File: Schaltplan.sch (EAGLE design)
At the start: 58 parts, among them Q1 TN0602N3, Q10 TN0602N3, Q11 TN0602N3, Q12 TN0602N3, Q13 TN0602N3, Q14 TN0602N3, Q15 TN0602N3, Q16 TN0602N3, Q17 TN0602N3, Q18 TN0602N3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

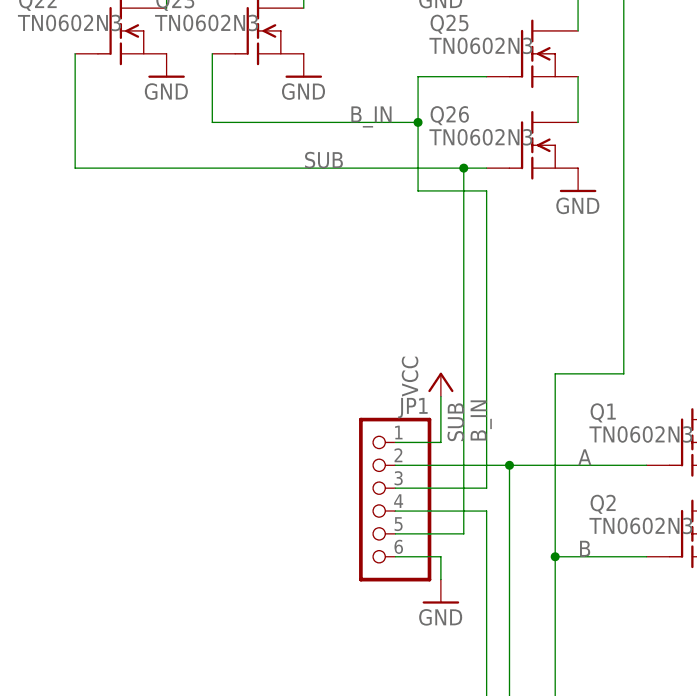
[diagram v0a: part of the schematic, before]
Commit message: Added Pull-Up Resistors
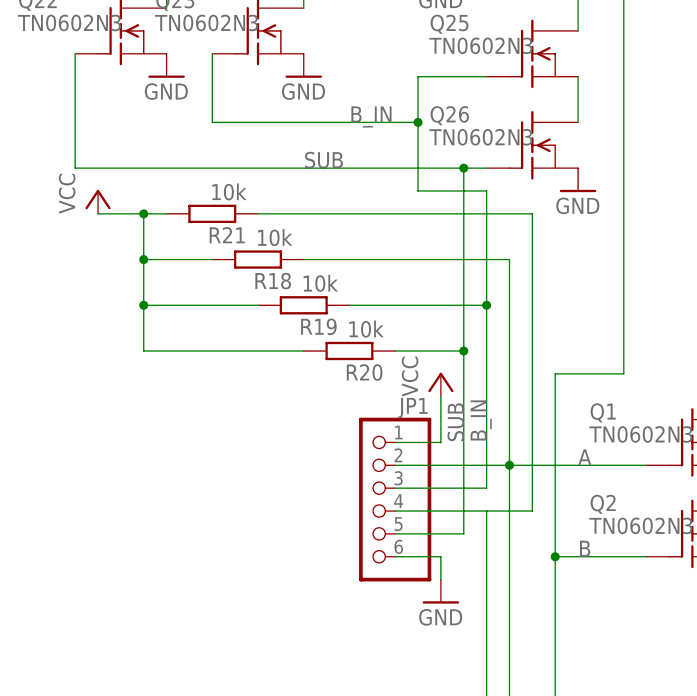
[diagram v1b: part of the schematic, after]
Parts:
- removed U$1, U$2: LOGO, logo:LOGO
- added R18, R19, R20, R21: 10k, resistor:R-EU_M0805
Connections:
- net A: now also R18.1
- net B_IN: now also R19.1
- net C_IN: now also R21.1
- net SUB: now also R20.1
- net VCC: now also R18.2, R19.2, R20.2, R21.2
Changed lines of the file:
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@@
 <part name="GND27" library="supply1" deviceset="GND" device=""/>
 <part name="GND28" library="supply1" deviceset="GND" device=""/>
-<part name="U$1" library="logo" deviceset="LOGO" device=""/>
-<part name="U$2" library="logo" deviceset="LOGO" device=""/>
 <part name="U$3" library="logo" deviceset="LOGO" device=""/>
+<part name="R18" library="resistor" deviceset="R-EU_" device="M0805" value="10k"/>
+<part name="R19" library="resistor" deviceset="R-EU_" device="M0805" value="10k"/>
+<part name="R20" library="resistor" deviceset="R-EU_" device="M0805" value="10k"/>
+<part name="R21" library="resistor" deviceset="R-EU_" device="M0805" value="10k"/>
+<part name="P+23" library="supply1" deviceset="VCC" device=""/>
 </parts>
 <sheets>
@@
 <instance part="GND28" gate="1" x="139.7" y="144.78"/>
 <instance part="U$3" gate="G$1" x="2.54" y="45.72"/>
+<instance part="R18" gate="G$1" x="7.62" y="114.3" rot="R180"/>
+<instance part="R19" gate="G$1" x="12.7" y="109.22" rot="R180"/>
+<instance part="R20" gate="G$1" x="17.78" y="104.14" rot="R180"/>
+<instance part="R21" gate="G$1" x="2.54" y="119.38" rot="R180"/>
+<instance part="P+23" gate="VCC" x="-10.16" y="121.92"/>
 </instances>
 <busses>
@@
 <pinref part="P+22" gate="VCC" pin="VCC"/>
 </segment>
+<segment>
+<pinref part="R21" gate="G$1" pin="2"/>
+<wire x1="-2.54" y1="119.38" x2="-5.08" y2="119.38" width="0.1524" layer="91"/>
+<pinref part="P+23" gate="VCC" pin="VCC"/>
+<pinref part="R20" gate="G$1" pin="2"/>
+<wire x1="-5.08" y1="119.38" x2="-10.16" y2="119.38" width="0.1524" layer="91"/>
+<wire x1="12.7" y1="104.14" x2="-5.08" y2="104.14" width="0.1524" layer="91"/>
+<wire x1="-5.08" y1="104.14" x2="-5.08" y2="109.22" width="0.1524" layer="91"/>
+<pinref part="R19" gate="G$1" pin="2"/>
+<wire x1="-5.08" y1="109.22" x2="-5.08" y2="114.3" width="0.1524" layer="91"/>
+<wire x1="-5.08" y1="114.3" x2="-5.08" y2="119.38" width="0.1524" layer="91"/>
+<wire x1="7.62" y1="109.22" x2="-5.08" y2="109.22" width="0.1524" layer="91"/>
+<pinref part="R18" gate="G$1" pin="2"/>
+<wire x1="2.54" y1="114.3" x2="-5.08" y2="114.3" width="0.1524" layer="91"/>
+<junction x="-5.08" y="109.22"/>
+<junction x="-5.08" y="114.3"/>
+<junction x="-5.08" y="119.38"/>
+</segment>
 </net>
 <net name="N$3" class="0">
@@
 <label x="58.42" y="53.34" size="1.778" layer="95"/>
 <pinref part="JP1" gate="A" pin="2"/>
+<pinref part="R18" gate="G$1" pin="1"/>
+<wire x1="12.7" y1="114.3" x2="35.56" y2="114.3" width="0.1524" layer="91"/>
+<wire x1="35.56" y1="114.3" x2="35.56" y2="91.44" width="0.1524" layer="91"/>
 </segment>
 <segment>
@@
 <pinref part="JP1" gate="A" pin="4"/>
 <wire x1="22.86" y1="86.36" x2="33.02" y2="86.36" width="0.1524" layer="91"/>
+<wire x1="33.02" y1="86.36" x2="38.1" y2="86.36" width="0.1524" layer="91"/>
+<wire x1="38.1" y1="86.36" x2="38.1" y2="119.38" width="0.1524" layer="91"/>
+<pinref part="R21" gate="G$1" pin="1"/>
+<wire x1="38.1" y1="119.38" x2="7.62" y2="119.38" width="0.1524" layer="91"/>
 </segment>
 <segment>
@@
 <pinref part="JP1" gate="A" pin="5"/>
 <wire x1="22.86" y1="83.82" x2="30.48" y2="83.82" width="0.1524" layer="91"/>
-<wire x1="30.48" y1="83.82" x2="30.48" y2="124.46" width="0.1524" layer="91"/>
+<wire x1="30.48" y1="83.82" x2="30.48" y2="104.14" width="0.1524" layer="91"/>
 <junction x="30.48" y="124.46"/>
 <label x="30.48" y="93.98" size="1.778" layer="95" rot="R90"/>
+<pinref part="R20" gate="G$1" pin="1"/>
+<wire x1="30.48" y1="104.14" x2="30.48" y2="124.46" width="0.1524" layer="91"/>
+<wire x1="22.86" y1="104.14" x2="30.48" y2="104.14" width="0.1524" layer="91"/>
+<junction x="30.48" y="104.14"/>
 </segment>
 <segment>
@@
 <pinref part="JP1" gate="A" pin="3"/>
 <wire x1="22.86" y1="88.9" x2="33.02" y2="88.9" width="0.1524" layer="91"/>
-<wire x1="33.02" y1="88.9" x2="33.02" y2="121.92" width="0.1524" layer="91"/>
+<wire x1="33.02" y1="88.9" x2="33.02" y2="109.22" width="0.1524" layer="91"/>
 <pinref part="Q25" gate="G$1" pin="G"/>
+<wire x1="33.02" y1="109.22" x2="33.02" y2="121.92" width="0.1524" layer="91"/>
 <wire x1="33.02" y1="134.62" x2="25.4" y2="134.62" width="0.1524" layer="91"/>
 <wire x1="25.4" y1="134.62" x2="25.4" y2="129.54" width="0.1524" layer="91"/>
@@
 <label x="17.78" y="129.54" size="1.778" layer="95"/>
 <label x="33.02" y="93.98" size="1.778" layer="95" rot="R90"/>
-</segment>
-</net>
+<pinref part="R19" gate="G$1" pin="1"/>
+<wire x1="17.78" y1="109.22" x2="33.02" y2="109.22" width="0.1524" layer="91"/>
+<junction x="33.02" y="109.22"/>
+</segment>
+</net>
